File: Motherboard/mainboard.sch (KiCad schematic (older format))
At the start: 48 parts, among them IC1 BMX160, J1 Conn_01x01, J2 10118194-0001LF, J28 Conn_01x01, J29 Conn_01x01, J3 Micro_SD_Card, J30 Conn_01x01, J4 xf2m-2415-1a, J5 XF2M-1015-1A, SW1 KMR231NG LFS, U1 RFM95W-915S2, U2 ATSAMD51G_TQFN48, U3 DRV8848, U4 TPS82740BSIPR, U5 DRV8848, U6 MAX708RESA-T, U8 RFM95W-915S2, X1 ANTENNA_U.FL, X2 ANTENNA_U.FL

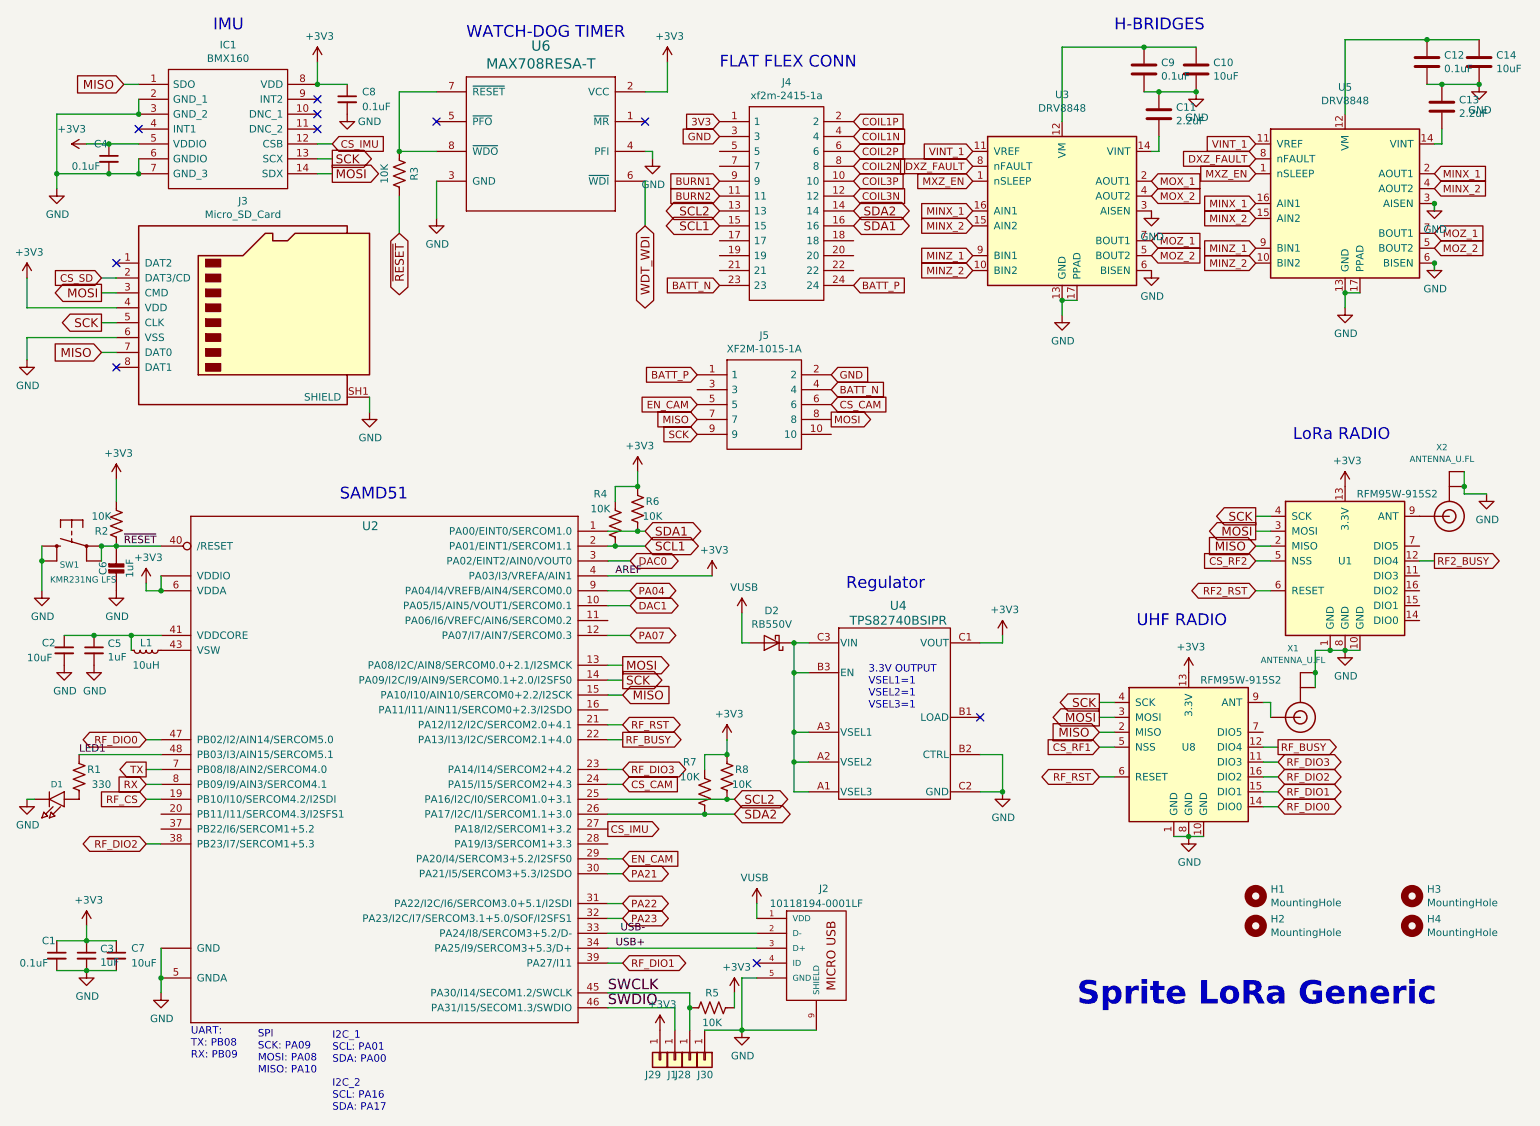
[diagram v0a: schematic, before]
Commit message: added SCL2 and SDA2 traces between MCU and flat flex connector
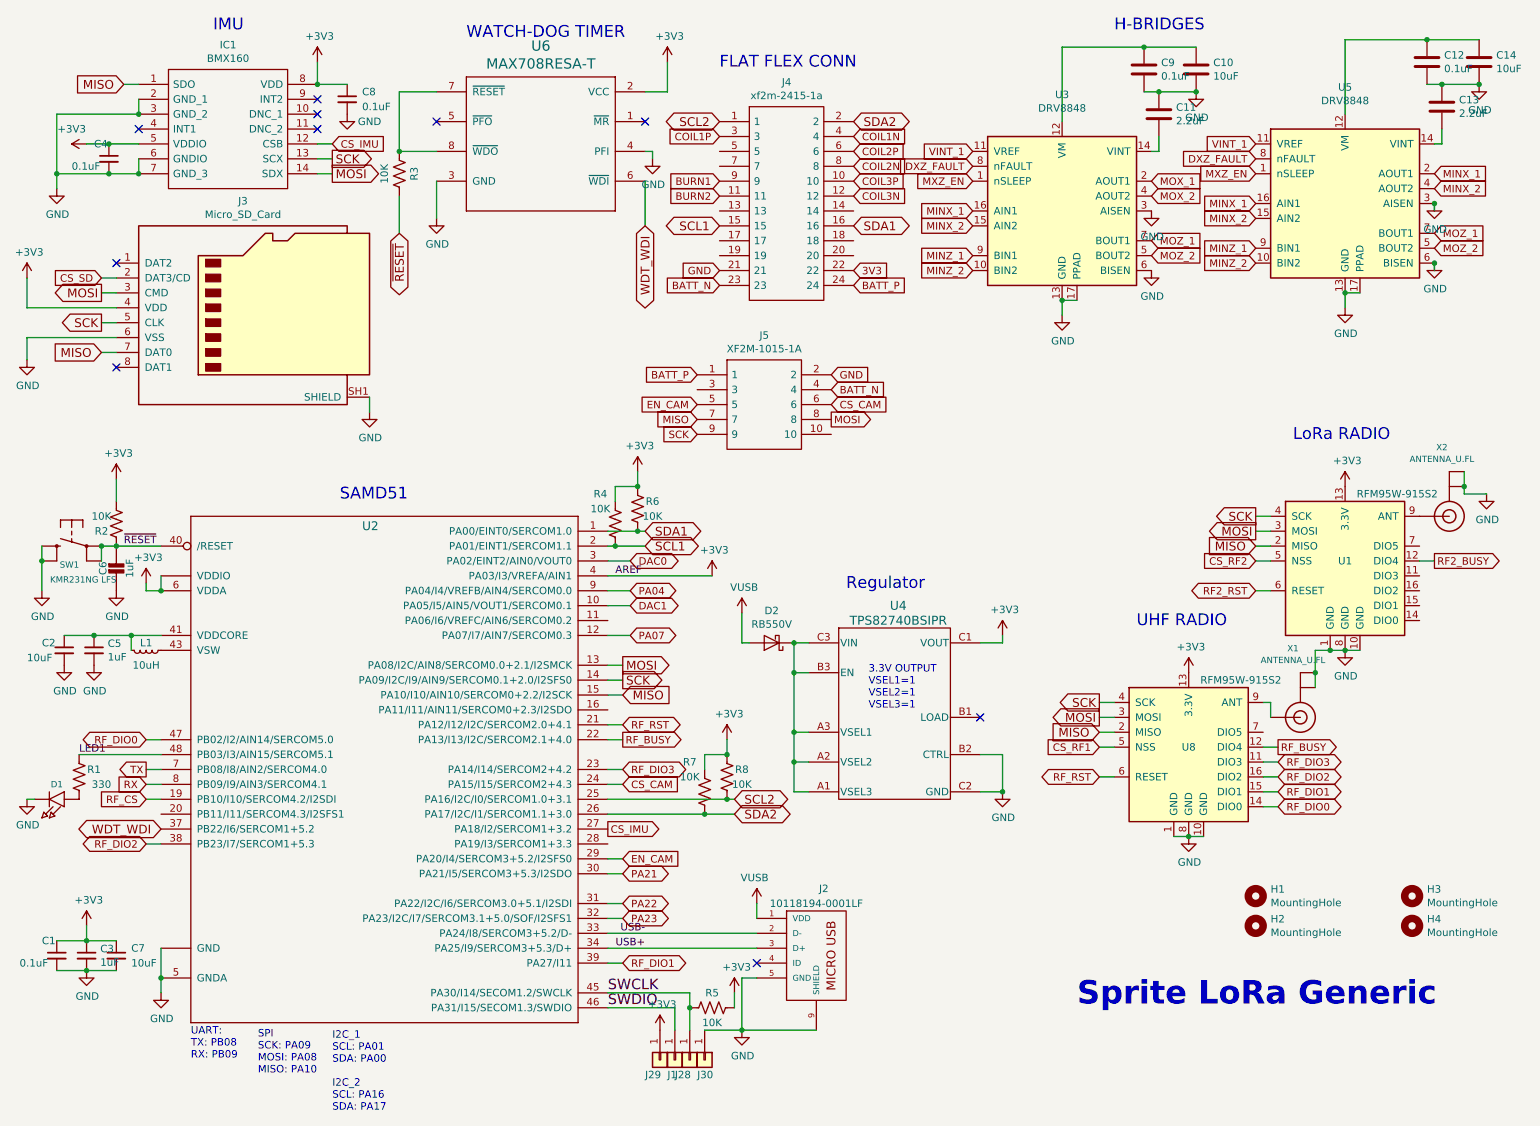
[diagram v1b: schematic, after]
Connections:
- net 3V3: now also J4.22; no longer J4.1
- net COIL1P: now also J4.3; no longer J4.2
- net GND: now also J4.21; no longer J4.3
- net SCL2: now also J4.1; no longer J4.13
- net SDA2: now also J4.2; no longer J4.14
- net WDT_WDI: now also U2.37 (PB22/I6/SERCOM1+5.2)
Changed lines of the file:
@@
 Text GLabel 5300 5800 2    59   BiDi ~ 0
 SCL2
-Text GLabel 5200 1250 0    50   Input ~ 0
+Text GLabel 6100 2250 2    50   Input ~ 0
 3V3
-Text GLabel 5200 1350 0    50   Input ~ 0
+Text GLabel 5200 2250 0    50   Input ~ 0
 GND
 Text GLabel 6100 2350 2    50   Input ~ 0
@@
 Text GLabel 5200 1750 0    50   Input ~ 0
 BURN2
-Text GLabel 6100 1250 2    50   Input ~ 0
+Text GLabel 5200 1350 0    50   Input ~ 0
 COIL1P
 Text GLabel 6100 1350 2    50   Input ~ 0
@@
 Text GLabel 5200 1950 0    59   BiDi ~ 0
 SCL1
-Text GLabel 5200 1850 0    59   BiDi ~ 0
+Text GLabel 5200 1250 0    59   BiDi ~ 0
 SCL2
-Text GLabel 6100 1850 2    59   BiDi ~ 0
+Text GLabel 6100 1250 2    59   BiDi ~ 0
 SDA2
 Wire Wire Line
@@
 Text GLabel 5050 2950 0    50   Input ~ 0
 BATT_P
+Text GLabel 1450 6000 0    59   BiDi ~ 0
+WDT_WDI
 $EndSCHEMATC

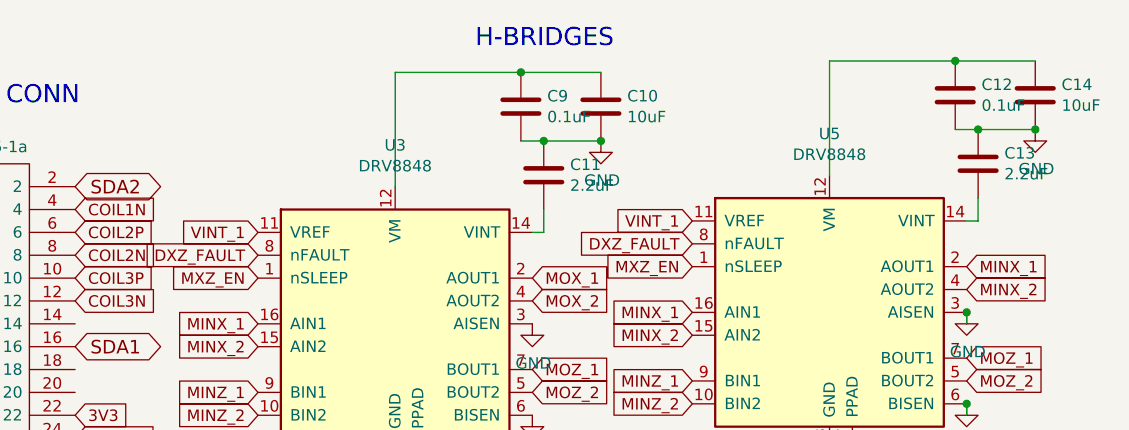
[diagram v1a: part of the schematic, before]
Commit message: updated H-bridge voltage nests on schematic, updated traces on PCB for H-bridges to flat flex connector and for watchdog timer
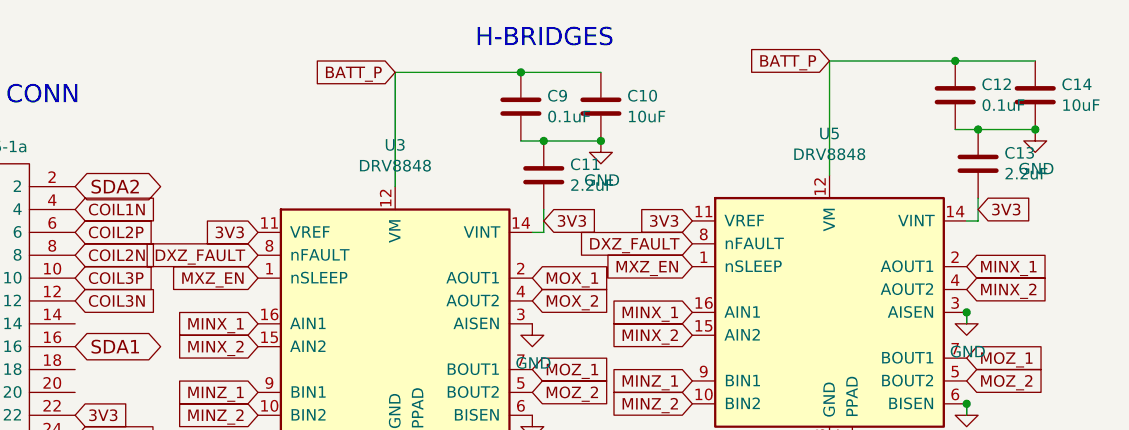
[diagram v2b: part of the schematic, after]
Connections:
- net VINT_1 is gone; now on net 3V3: U3.11 (VREF), U5.11 (VREF)
- net 3V3: now also C11.2, C13.2, U3.14 (VINT), U5.14 (VINT)
- net BATT_P: now also C10.1, C12.1, C14.1, C9.1, U3.12 (VM), U5.12 (VM)
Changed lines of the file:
@@
 	1    0    0    -1
 $EndComp
-Text GLabel 6900 1450 0    50   Input ~ 0
-VINT_1
 Text GLabel 6900 1550 0    50   Input ~ 0
 DXZ_FAULT
@@
 	1    0    0    -1
 $EndComp
-Text GLabel 8800 1400 0    50   Input ~ 0
-VINT_1
 Text GLabel 8800 1500 0    50   Input ~ 0
 DXZ_FAULT
@@
 Text GLabel 1450 6000 0    59   BiDi ~ 0
 WDT_WDI
+Text GLabel 7500 750  0    50   Input ~ 0
+BATT_P
+Text GLabel 9400 700  0    50   Input ~ 0
+BATT_P
+Text GLabel 6900 1450 0    50   Input ~ 0
+3V3
+Text GLabel 8150 1400 2    50   Input ~ 0
+3V3
+Text GLabel 8800 1400 0    50   Input ~ 0
+3V3
+Text GLabel 10050 1350 2    50   Input ~ 0
+3V3
 $EndSCHEMATC
